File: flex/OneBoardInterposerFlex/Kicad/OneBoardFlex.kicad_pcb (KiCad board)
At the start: 2 copper layers, 99.6 x 58.8 mm, 28 parts, among them J1 GT-USB-7010ASV, SW1 TS-1187A-C-A-B, U1 RT9013-33GB-MS, U3 W25Q16JVUXIQ, U4 RP2040, Y1 ABM8-272-T3

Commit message: PCB Attribution Update
- added explicit attribution to silverstone
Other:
- board text added: "PCB Layout By silverstone / Mitch Cairns"
- board text removed: "PCB Layout By Mitch Cairns"
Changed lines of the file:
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@@
 		(layer "Edge.Cuts")
 	)
-	(gr_text "PCB Layout By Mitch Cairns"
+	(gr_text "PCB Layout By silverstone / Mitch Cairns"
 		(at 155.0162 108.1024 0)
 		(layer "F.SilkS")
@@
 		)
 	)
-	(gr_text "PCB Layout By Mitch Cairns"
-		(at 157.29498 108.0262 -0)
-		(layer "B.SilkS")
-		(effects
-			(font
-				(size 1 1)
-			)
-			(justify mirror)
-		)
-	)
 	(gr_text "https://github.com/makeo/PicoLoader"
 		(at 157.06638 105.6386 -0)
@@
 			)
 			(justify mirror)
+		)
+	)
+	(gr_text "PCB Layout By silverstone / Mitch Cairns"
+		(at 154.686 108.0516 -0)
+		(layer "B.SilkS")
+		(effects
+			(font
+				(size 1 1)
+			)
+			(justify mirror)

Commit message: Fix silversteel's name
- This is why I shouldn't be working on projects past 1am
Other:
- board text added: "PCB Layout By silversteel / Mitch Cairns"
- board text removed: "PCB Layout By silverstone / Mitch Cairns"
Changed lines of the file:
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@@
 		(layer "Edge.Cuts")
 	)
-	(gr_text "PCB Layout By silverstone / Mitch Cairns"
+	(gr_text "PCB Layout By silversteel / Mitch Cairns"
 		(at 155.0162 108.1024 0)
 		(layer "F.SilkS")
@@
 		)
 	)
-	(gr_text "PCB Layout By silverstone / Mitch Cairns"
-		(at 154.686 108.0516 -0)
+	(gr_text "PCB Layout By silversteel / Mitch Cairns"
+		(at 154.686 108.0516 0)
 		(layer "B.SilkS")
 		(effects

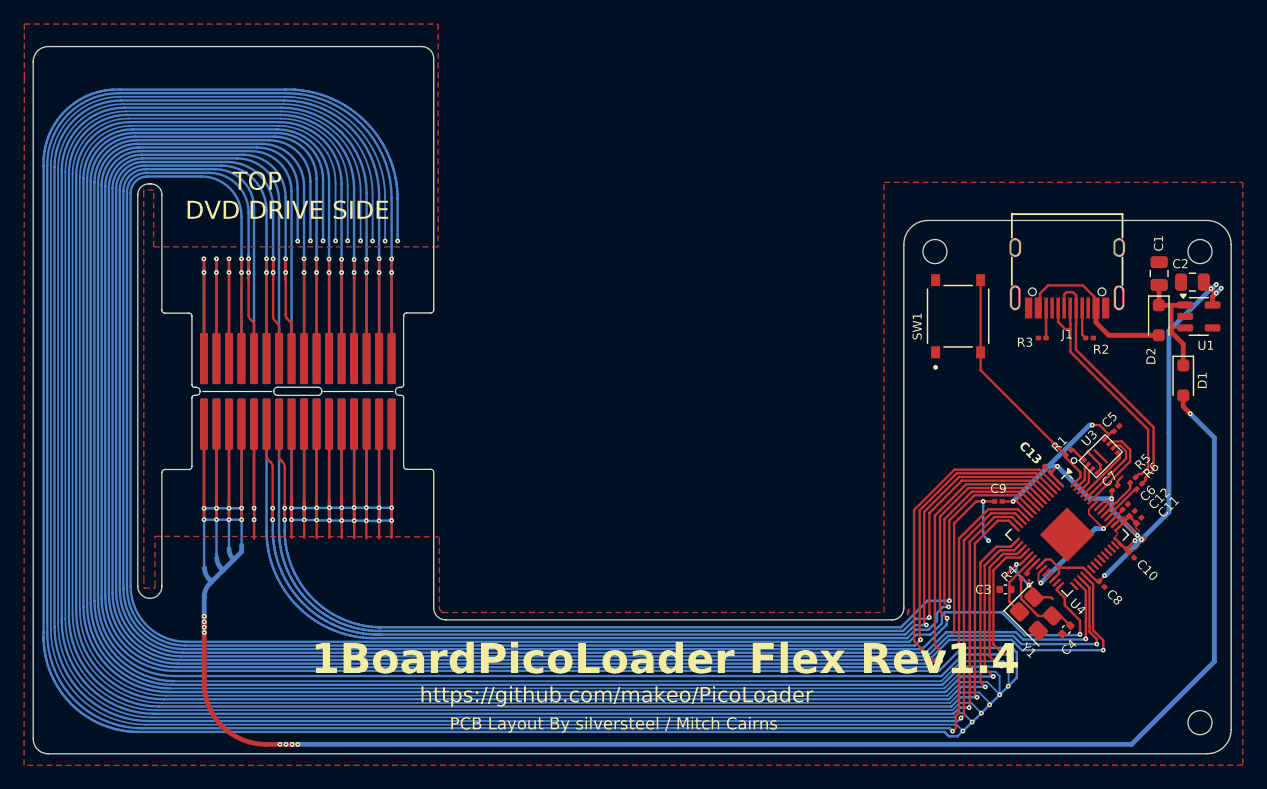
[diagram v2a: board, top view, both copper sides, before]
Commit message: Update board per suggested changes
- Replace components with JLCPCB basic components where possible
- Implement Red LED for GPIO25
- Adjust revision to Rev1.0
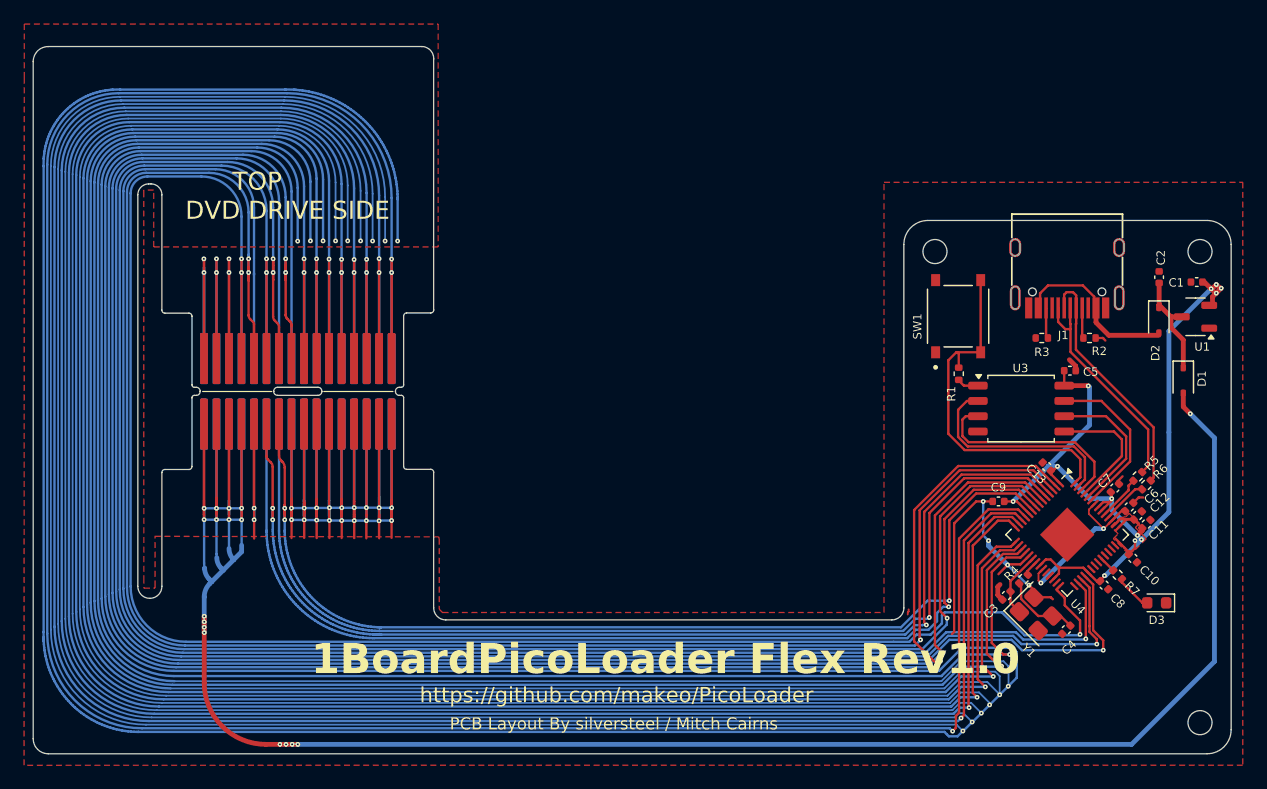
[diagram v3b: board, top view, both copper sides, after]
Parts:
- added D3: KT-0603R, LED_SMD:LED_0603_1608Metric, F.Cu at (200.2, 98.0)
- added R7: 470R, Resistor_SMD:R_0402_1005Metric, F.Cu at (196.9, 95.7)
- C1, C2: value 10uF -> 1uF; footprint Capacitor_SMD:C_0805_2012Metric -> Capacitor_SMD:C_0402_1005Metric
- C10, C11, C12, C13, C5, C6, C7, C8, C9: footprint Capacitor_SMD:C_0201_0603Metric -> Capacitor_SMD:C_0402_1005Metric
- D1, D2: value CUS08F30,H3F -> 1N5819WS; footprint Diode_SMD:D_SOD-323_HandSoldering -> Diode_SMD:D_SOD-323
- R1, R2, R3, R4, R5, R6: footprint Resistor_SMD:R_0201_0603Metric -> Resistor_SMD:R_0402_1005Metric
- SW1: value TS-1187A-C-A-B -> TS-1187A-B-A-B
- U1: value RT9013-33GB-MS -> XC6206P332MR-G; footprint Package_TO_SOT_SMD:SOT-23-5 -> Package_TO_SOT_SMD:SOT-23-3
- U3: value W25Q16JVUXIQ -> W25Q128JVSIQ; footprint hhl:USON-8-EP(2x3) -> Package_SO:SOIC-8_5.3x5.3mm_P1.27mm
- moved R1 11.2 mm to (183.7, 79.0), turned to -90 degrees
- moved U3 7.72 mm to (188.9, 81.9), turned to 0 degrees
- moved C5 6.20 mm to (192.9, 78.7), turned to 0 degrees
- moved C1 3.20 mm to (203.5, 71.4), turned to 0 degrees
- moved C2 2.80 mm to (200.4, 71.0), turned to -90 degrees
- moved C11 0.70 mm to (199.3, 91.5)
- moved R6 0.60 mm to (199.3, 88.2)
- moved C3 0.51 mm to (187.7, 97.4), turned to -135 degrees
- moved R5 0.51 mm to (198.6, 87.5)
- moved C12 0.51 mm to (198.6, 90.8)
- moved C6 0.33 mm to (197.9, 90.1)
- moved C10 0.31 mm to (198.2, 94.3)
- moved U1 0.28 mm to (203.4, 74.3), turned to 180 degrees
- moved R4 0.27 mm to (189.1, 96.1)
- moved C13 0.24 mm to (191.0, 86.7)
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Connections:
- C1 pad 2: VBUS -> +3V3
- C2 pad 1: +3V3 -> GND
- C2 pad 2: GND -> VBUS
- U1 pad 1: VBUS -> GND
- U1 pad 2: GND -> +3V3
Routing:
- net SIO1: track 2.23 -> 18.1 mm
- net SIO2: track 2.19 -> 17.5 mm
- net USB_BOOT: track 20.5 -> 30.4 mm
- net SIO0: track 4.71 -> 10.9 mm
- net SIO3: track 7.67 -> 13.7 mm
- net SCLK: track 6.48 -> 12.2 mm
- net GND: track 1606.2 -> 1611.5 mm
- net +3V3: track 77.2 -> 81.4 mm
- net Net-(D3-A): track 0.00 -> 3.08 mm
- net VBUS: track 10.5 -> 8.64 mm
- net /GPIO25: track 0.00 -> 1.38 mm
- net D+: track 19.8 -> 19.0 mm
- net D-: track 21.1 -> 20.5 mm
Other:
- board text added: "1BoardPicoLoader Flex Rev1.0"
- board text removed: "1BoardPicoLoader Flex Rev1.4"

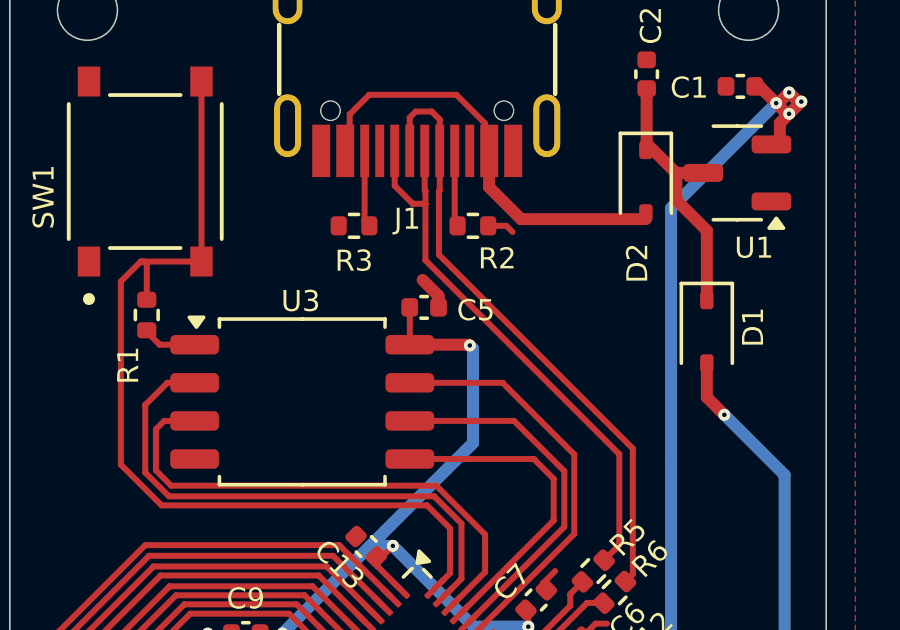
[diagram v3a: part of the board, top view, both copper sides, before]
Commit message: 27ohm -> 22 ohm for USB resistors
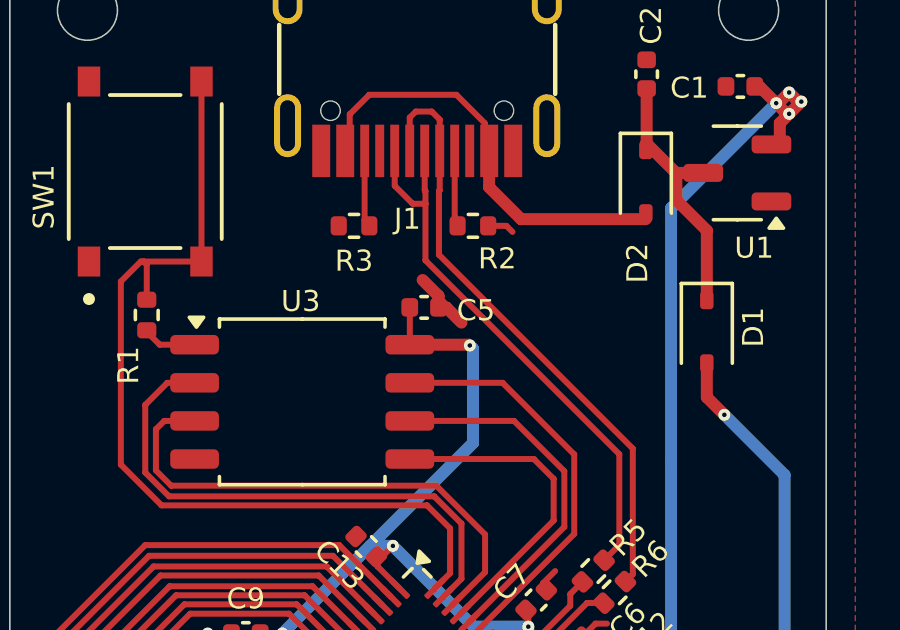
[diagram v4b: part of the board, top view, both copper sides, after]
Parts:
- R5, R6: value 27R -> 22R
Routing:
- net GND: track 1611.5 -> 1612.4 mm
